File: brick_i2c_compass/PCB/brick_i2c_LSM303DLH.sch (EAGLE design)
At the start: 12 parts

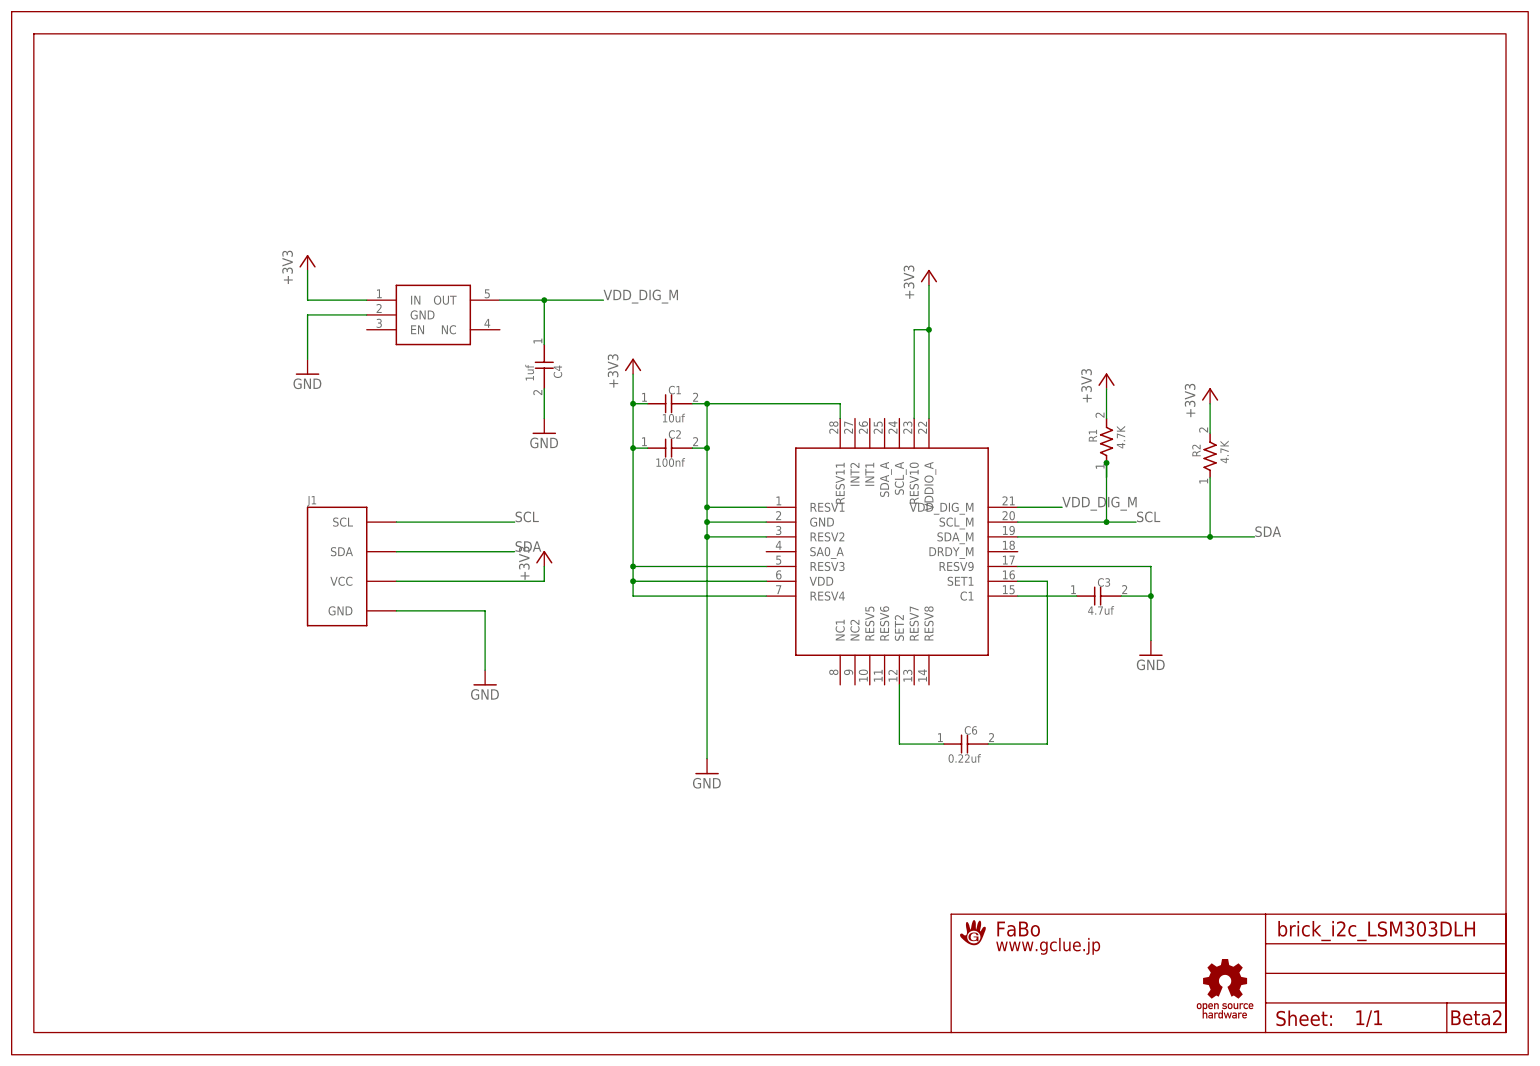
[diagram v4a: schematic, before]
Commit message: change logo
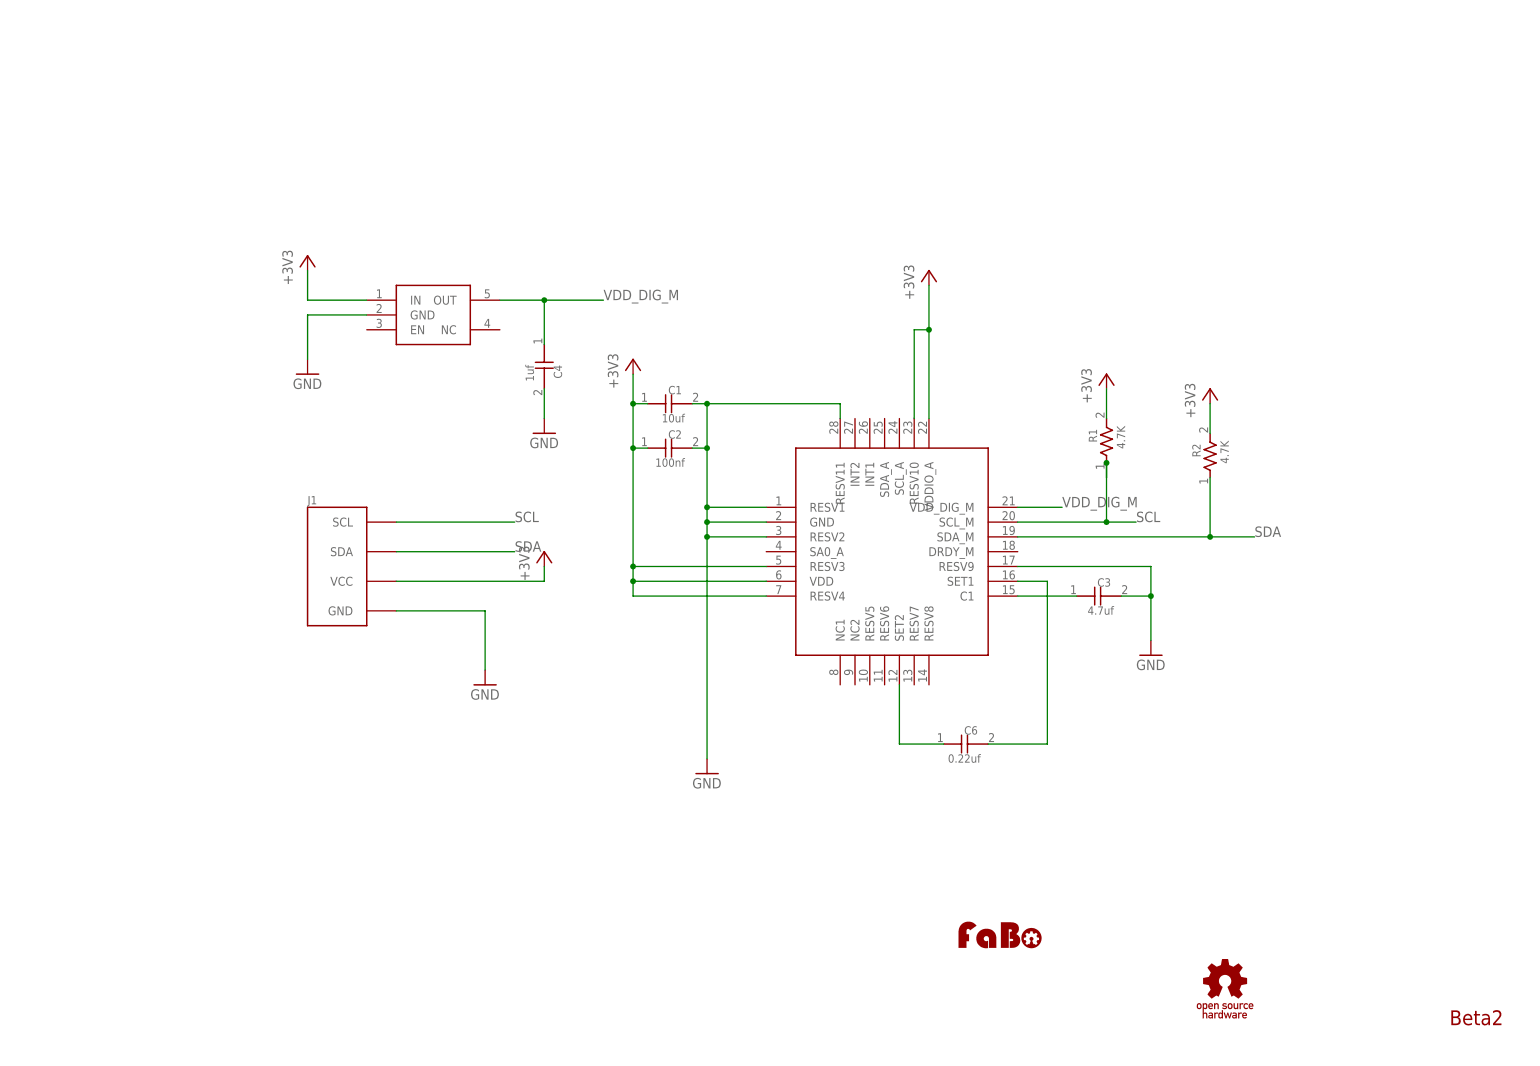
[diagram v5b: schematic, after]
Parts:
- removed U$1: A4L-LOC-FABO_M, gclue:A4L-LOC-FABO_M
- added U$5: (no value), FaBo:LOGO_FABO-M
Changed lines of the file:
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@@
 </classes>
 <parts>
-<part name="U$1" library="gclue" deviceset="A4L-LOC" device="-FABO_M"/>
+<part name="U$1" library="gclue" deviceset="A4L-LOC" device=""/>
 <part name="GND1" library="supply1" deviceset="GND" device=""/>
 <part name="GND2" library="supply1" deviceset="GND" device=""/>
@@
 <part name="J1" library="gclue" deviceset="BRICK_I2C" device=""/>
 <part name="U$4" library="gclue" deviceset="LOGO_OSHW_T" device="-M"/>
+<part name="U$5" library="FaBo" deviceset="LOGO_FABO" device="-M"/>
 </parts>
 <sheets>
@@
 <instance part="J1" gate="G$1" x="58.42" y="83.82"/>
 <instance part="U$4" gate="G$1" x="208.28" y="12.7"/>
+<instance part="U$5" gate="G$1" x="162.56" y="22.86"/>
 </instances>
 <busses>
